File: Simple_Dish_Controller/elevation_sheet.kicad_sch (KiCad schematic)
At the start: 20 parts, among them J2 1-Pin Terminal Block, J7 RJ45 port shielded, RA, TH, J8 RJ45 port shielded, RA, TH, Q1 PZT2222A, Q2 PZT2222A, SW2 SW_SPDT_312, U2 74LS08, U3 74LS32, U4 NE555PS

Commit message: Still creating parts libraries
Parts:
- removed SW2: SW_SPDT_312, SPDT-90-Deg-On-Off-On:B18JH, symbol Switch:SW_SPDT_312
- added J6: Conn_01x03_Pin, DishFootprints:PinHeader_1x03_P2.54mm_Vertical, symbol DishSymbols:Conn_01x03_Pin
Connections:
- net +5V: now also J6.2
- net Dir Sig: now also J6.1
- net at R5.1, U2.5: now also J6.3
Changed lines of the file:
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@@
+	(wire
+		(pts
+			(xy 54.61 58.42) (xy 54.61 67.31)
+		)
+		(stroke
+			(width 0)
+			(type default)
+		)
+	)
 	(wire
 		(pts
@@
 	(wire
 		(pts
+			(xy 52.07 67.31) (xy 54.61 67.31)
+		)
+		(stroke
+			(width 0)
+			(type default)
+		)
+	)
+	(wire
+		(pts
 			(xy 228.6 53.34) (xy 236.22 53.34)
 		)
@@
 	(wire
 		(pts
-			(xy 48.26 67.31) (xy 43.18 67.31)
-		)
-		(stroke
-			(width 0)
-			(type default)
-		)
-	)
-	(wire
-		(pts
 			(xy 96.52 66.04) (xy 104.14 66.04)
 		)
@@
 	(wire
 		(pts
+			(xy 52.07 69.85) (xy 58.42 69.85)
+		)
+		(stroke
+			(width 0)
+			(type default)
+		)
+	)
+	(wire
+		(pts
 			(xy 195.58 50.8) (xy 195.58 52.07)
 		)
@@
 	(wire
 		(pts
+			(xy 52.07 64.77) (xy 58.42 64.77)
+		)
+		(stroke
+			(width 0)
+			(type default)
+		)
+	)
+	(wire
+		(pts
 			(xy 232.41 82.55) (xy 238.76 82.55)
 		)
@@
 		(pts
 			(xy 214.63 137.16) (xy 214.63 139.7)
-		)
-		(stroke
-			(width 0)
-			(type default)
-		)
-	)
-	(wire
-		(pts
-			(xy 43.18 67.31) (xy 43.18 62.23)
 		)
 		(stroke
@@
 	(symbol
 		(lib_id "power:+5V")
-		(at 43.18 62.23 0)
+		(at 54.61 58.42 0)
 		(unit 1)
 		(exclude_from_sim no)
@@
 		(dnp no)
 		(property "Reference" "#PWR09"
-			(at 43.18 66.04 0)
+			(at 54.61 62.23 0)
 			(effects
 				(font
@@
 		)
 		(property "Value" "+5V"
-			(at 43.18 58.42 0)
+			(at 54.61 54.61 0)
 			(effects
 				(font
@@
 		)
 		(property "Footprint" ""
-			(at 43.18 62.23 0)
+			(at 54.61 58.42 0)
 			(effects
 				(font
@@
 		)
 		(property "Datasheet" ""
-			(at 43.18 62.23 0)
+			(at 54.61 58.42 0)
 			(effects
 				(font
@@
 		)
 		(property "Description" "Power symbol creates a global label with name \"+5V\""
-			(at 43.18 62.23 0)
+			(at 54.61 58.42 0)
 			(effects
 				(font
@@
 	)
 	(symbol
+		(lib_id "DishSymbols:Conn_01x03_Pin")
+		(at 46.99 67.31 0)
+		(unit 1)
+		(exclude_from_sim no)
+		(in_bom yes)
+		(on_board yes)
+		(dnp no)
+		(property "Reference" "J6"
+			(at 46.99 62.23 0)
+			(effects
+				(font
+					(size 1.27 1.27)
+				)
+			)
+		)
+		(property "Value" "Conn_01x03_Pin"
+			(at 46.99 72.39 0)
+			(effects
+				(font
+					(size 1.27 1.27)
+				)
+			)
+		)
+		(property "Footprint" "DishFootprints:PinHeader_1x03_P2.54mm_Vertical"
+			(at 46.99 67.31 0)
+			(effects
+				(font
+					(size 1.27 1.27)
+				)
+				(hide yes)
+			)
+		)
+		(property "Datasheet" "~https://app.adam-tech.com/products/download/data_sheet/201605/ph1-xx-ua-data-sheet.pdf"
+			(at 46.99 67.31 0)
+			(effects
+				(font
+					(size 1.27 1.27)
+				)
+				(hide yes)
+			)
+		)
+		(property "Description" "Connector Header Through Hole 3 position 0.100\" (2.54mm)"
+			(at 46.99 67.31 0)
+			(effects
+				(font
+					(size 1.27 1.27)
+				)
+				(hide yes)
+			)
+		)
+		(property "Package" "-"
+			(at 46.99 67.31 0)
+			(effects
+				(font
+					(size 1 1)
+				)
+				(hide yes)
+			)
+		)
+		(property "MF" "Adam Tech"
+			(at 46.99 67.31 0)
+			(effects
+				(font
+					(size 1 1)
+				)
+				(hide yes)
+			)
+		)
+		(property "MPN" "PH1-03-UA"
+			(at 46.99 67.31 0)
+			(effects
+				(font
+					(size 1 1)
+				)
+				(hide yes)
+			)
+		)
+		(property "DIS" "Digikey"
+			(at 46.99 67.31 0)
+			(effects
+				(font
+					(size 1 1)
+				)
+				(hide yes)
+			)
+		)
+		(property "DPN" "2057-PH1-03-UA-ND"
+			(at 46.99 67.31 0)
+			(effects
+				(font
+					(size 1 1)
+				)
+				(hide yes)
+			)
+		)
+		(property "Purchase_URL" "https://www.digikey.com/en/products/detail/adam-tech/PH1-03-UA/9830289"
+			(at 46.99 67.31 0)
+			(effects
+				(font
+					(size 1 1)
+				)
+				(hide yes)
+			)
+		)
+		(property "Price" "0.04"
+			(at 46.99 67.31 0)
+			(effects
+				(font
+					(size 1 1)
+				)
+				(hide yes)
+			)
+		)
+		(property "Note" ""
+			(at 46.99 67.31 0)
+			(effects
+				(font
+					(size 1 1)
+				)
+				(hide yes)
+			)
+		)
+		(pin "3"
+		)
+		(pin "1"
+		)
+		(pin "2"
+		)
+		(instances
+			(project ""
+				(path "/8648ccd3-30ce-4b98-baff-aeab56a7c9f5/a4809f50-064d-4cb7-b1f7-56bf09fb0ea4"
+					(reference "J6")
+					(unit 1)
+				)
+			)
+		)
+	)
+	(symbol
 		(lib_id "power:GND")
 		(at 69.85 172.72 0)
@@
 					(unit 1)
 				)
-			)
-		)
-	)
-	(symbol
-		(lib_id "Switch:SW_SPDT_312")
-		(at 53.34 67.31 0)
-		(unit 1)
-		(exclude_from_sim no)
-		(in_bom yes)
-		(on_board yes)
-		(dnp no)
-		(property "Reference" "SW2"
-			(at 53.34 62.23 0)
-			(effects
-				(font
-					(size 1.27 1.27)
-				)
-			)
-		)
-		(property "Value" "SW_SPDT_312"
-			(at 53.34 60.96 0)
-			(effects
-				(font
-					(size 1.27 1.27)
-				)
-				(hide yes)
-			)
-		)
-		(property "Footprint" "SPDT-90-Deg-On-Off-On:B18JH"
-			(at 53.34 77.47 0)
-			(effects
-				(font
-					(size 1.27 1.27)
-				)
-				(hide yes)
-			)
-		)
-		(property "Datasheet" "~"
-			(at 53.34 74.93 0)
-			(effects
-				(font
-					(size 1.27 1.27)
-				)
-				(hide yes)
-			)
-		)
-		(property "Description" "Switch, single pole double throw"
-			(at 53.34 67.31 0)
-			(effects
-				(font
-					(size 1.27 1.27)
-				)
-				(hide yes)
-			)
-		)
-		(property "LCSC Part" ""
-			(at 53.34 67.31 0)
-			(effects
-				(font
-					(size 1.27 1.27)
-				)
-			)
-		)
-		(pin "2"
-		)
-		(pin "1"
-		)
-		(pin "3"
-		)
-		(instances
-			(project "simple_dish_manual_controller"
-				(path "/8648ccd3-30ce-4b98-baff-aeab56a7c9f5/a4809f50-064d-4cb7-b1f7-56bf09fb0ea4"
-					(reference "SW2")
-					(unit 1)
-				)

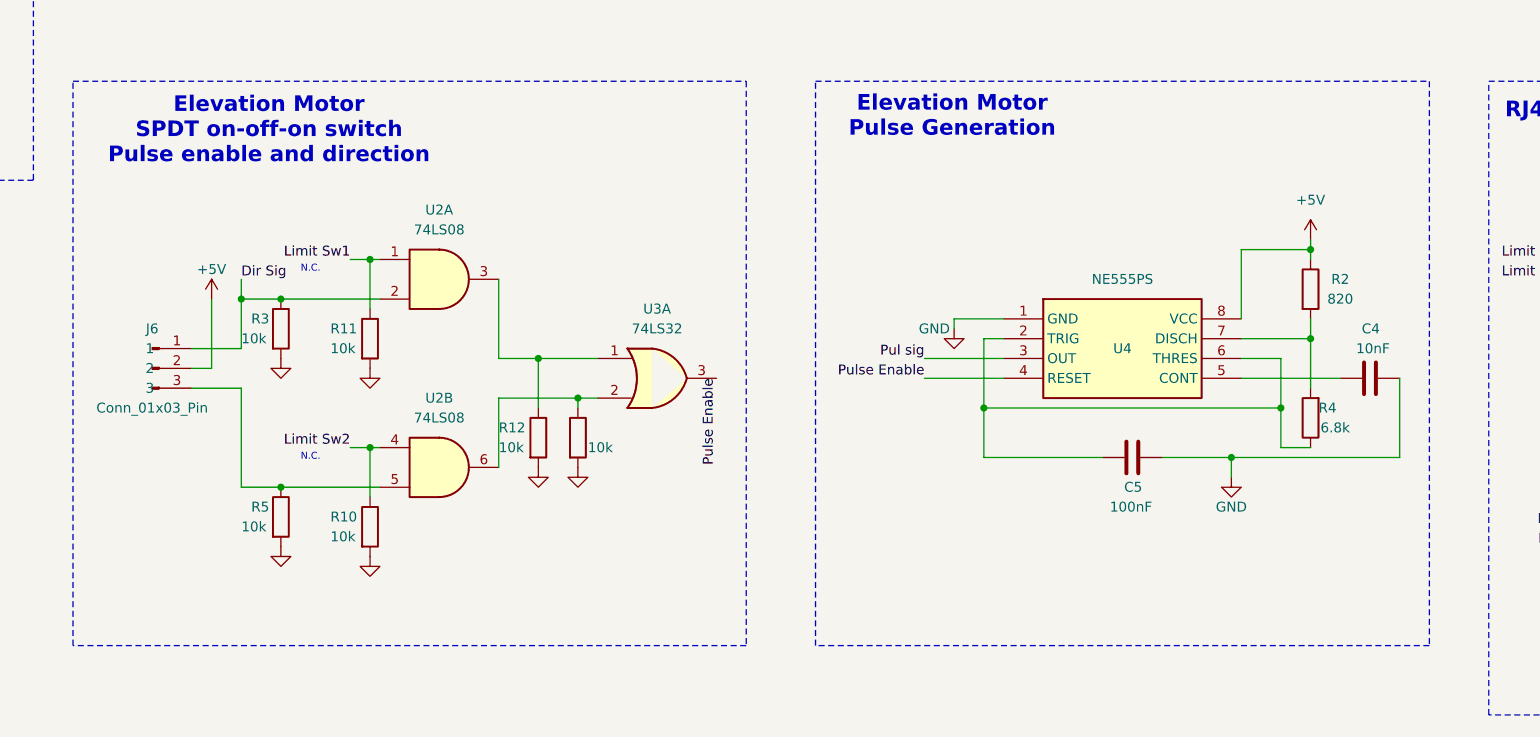
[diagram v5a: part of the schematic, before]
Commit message: More parts defined
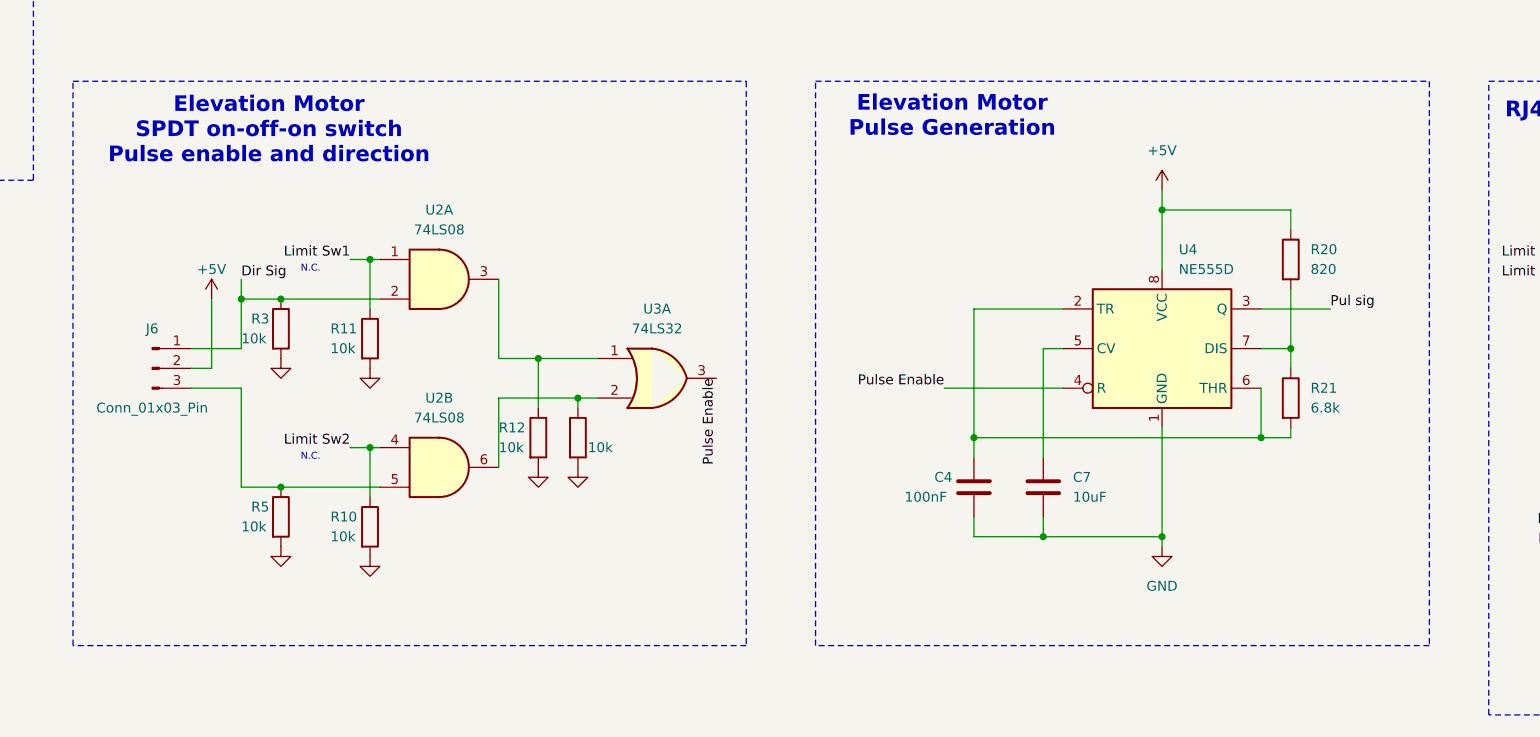
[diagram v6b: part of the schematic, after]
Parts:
- removed C4: 10nF, Capacitor_SMD:C_0805_2012Metric, symbol Device:C
- removed C5: 100nF, Capacitor_SMD:C_0805_2012Metric, symbol Device:C
- removed R2: 820, Resistor_SMD:R_0805_2012Metric, symbol Device:R
- removed R4: 6.8k, Resistor_SMD:R_0805_2012Metric, symbol Device:R
- removed U4: NE555PS, NE555P Osc Chip SMD:SOIC127P780X200-8N, symbol NE555P Osc Chip SMD:NE555PS
- added C4: 100nF, DishFootprints:C_0805, symbol DishSymbols:CAP 100nF 0805
- added C7: 10uF, DishFootprints:C_0805, symbol DishSymbols:CAP 10nF 0805
- added R20: 820, DishFootprints:R_0805, symbol DishSymbols:RES 820 0805
- added R21: 6.8k, DishFootprints:R_0805, symbol DishSymbols:RES 6.8k 0805
- added U4: NE555D, DishFootprints:SOIC-8_3.9x4.9mm_P1.27mm, symbol DishSymbols:NE555D
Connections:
- net +5V: now also R20.1, U4.8 (VCC)
- net GND: now also C4.2, C7.2, U4.1 (GND)
- net Pul sig: now also U4.3 (Q)
- net Pulse Enable: now also U4.4 (R)
- new net: R20.2, R21.1, U4.7 (DIS)
- new net: C4.1, R21.2, U4.2 (TR), U4.6 (THR)
- new net: C7.1, U4.5 (CV)

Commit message: Latest update
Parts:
- removed J2: 1-Pin Terminal Block, 1-Pin Barrier Terminal Block:RHDR1W160P0X826_1X1_1020X1270X1270P, symbol 1-Pin Barrier Terminal Block:38700-6301
- removed J7, J8: RJ45 port shielded, RA, TH, DishController_footprints:RJ45 Port Shielded, Right Angle TH, symbol DishController_symbols:RJ45 port shielded, Right Angle TH
- removed Q1, Q2: PZT2222A, Package_TO_SOT_SMD:SOT-223-3_TabPin2, symbol Transistor_BJT:PZT2222A
- removed U2: 74LS08, 74LS08_SOIC:SOIC127P600X175-14N, symbol 74xx:74LS08
- removed U3: 74LS32, 74LS32_SOIC:SOIC127P600X175-14N, symbol 74xx:74LS32
- added J5: DE-15_VGA_FEMALE_CONN, DishFootprintsSupplier:DB15_VGA_FEMALE_CONN, symbol DishSymbolsSupplier:DE-15_VGA_FEMALE_CONN
- added Q1, Q5: PZT2222A, DishFootprints:SOT-223, symbol DishSymbols:PZT2222A
- added U2: 74LS08, DishFootprints:SOIC-14_3.9x8.7mm_P1.27mm, symbol DishSymbols:74LS08
- added U3: 74LS32, DishFootprints:SOIC-14_3.9x8.7mm_P1.27mm, symbol DishSymbols:74LS32
- R13: footprint Resistor_SMD:R_0805_2012Metric -> DishFootprints:R_0805
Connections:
- net +5V: now also J5.1
- net Dir: now also J5.12, Q5.2 (C)
- net Dir Sig: now also U2.2
- net GND: now also J5.2, Q1.3 (E), Q5.3 (E)
- net Limit Sw1: now also J5.3, U2.1
- net Limit Sw2: now also J5.4, U2.4
- net Pul: now also J5.11, Q1.2 (C)
- net Pul sig: now also Q1.1 (B)
- net Pulse Enable: now also U3.3
- net Shield: now also J5.SH1 (SHIELD), J5.SH2 (SHIELD)
- net at R13.1: now also U2.6, U3.2
- net at J6.3, R5.1: now also U2.5
- net at R6.2: now also Q5.1 (B)
- net at R12.1: now also U2.3, U3.1
- no-connect marks 22 -> 9
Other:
- note removed: "Connect to Chassis"
- note removed: "Logic Chips Power and Gnd"
- note removed: "Shield to Chassis"
- note removed: "Unused from Quad chip"
- moved on the sheet: R6

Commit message: Updates
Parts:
- removed C4: 100nF, DishFootprints:C_0805, symbol DishSymbols:CAP 100nF 0805
- removed C7: 10uF, DishFootprints:C_0805, symbol DishSymbols:CAP 10nF 0805
- removed J5: DE-15_VGA_FEMALE_CONN, DishFootprintsSupplier:DB15_VGA_FEMALE_CONN, symbol DishSymbolsSupplier:DE-15_VGA_FEMALE_CONN
- removed J6: Conn_01x03_Pin, DishFootprints:PinHeader_1x03_P2.54mm_Vertical, symbol DishSymbols:Conn_01x03_Pin
- removed Q1, Q5: PZT2222A, DishFootprints:SOT-223, symbol DishSymbols:PZT2222A
- removed R11, R12: 10k, Resistor_SMD:R_0805_2012Metric, symbol Device:R
- removed R13: 10k, DishFootprints:R_0805, symbol Device:R
- removed R20: 820, DishFootprints:R_0805, symbol DishSymbols:RES 820 0805
- removed R21: 6.8k, DishFootprints:R_0805, symbol DishSymbols:RES 6.8k 0805
- removed U2: 74LS08, DishFootprints:SOIC-14_3.9x8.7mm_P1.27mm, symbol DishSymbols:74LS08
- removed U3: 74LS32, DishFootprints:SOIC-14_3.9x8.7mm_P1.27mm, symbol DishSymbols:74LS32
- removed U4: NE555D, DishFootprints:SOIC-8_3.9x4.9mm_P1.27mm, symbol DishSymbols:NE555D
- added C5: 0.1uF, Capacitor_SMD:C_1206_3216Metric, symbol Device:C
- added C6: 100nF, Capacitor_SMD:C_1206_3216Metric, symbol Device:C
- added C7: 10uF, Capacitor_SMD:C_1206_3216Metric, symbol Device:C
- added J4: Conn_01x03_Pin, Connector_PinHeader_2.54mm:PinHeader_1x03_P2.54mm_Vertical, symbol Connector:Conn_01x03_Pin
- added J5: Elevation DE-15, DishFootprints:DE15_VGA_FEMALE_CONN, symbol DishSymbols:DE-15_VGA_FEMALE_CONN
- added Q1, Q2: MMBT2222A, Package_TO_SOT_SMD:SOT-23, symbol Transistor_BJT:MMBT2222A
- added R2: 820, Resistor_SMD:R_1206_3216Metric, symbol Device:R
- added R4, R7, R8, R9: 10k, Resistor_SMD:R_1206_3216Metric, symbol Device:R
- added U2: 74LS32, Package_SO:SOIC-14_3.9x8.7mm_P1.27mm, symbol 74xx:74LS32
- added U3: 74LS08, Package_SO:SOIC-14_3.9x8.7mm_P1.27mm, symbol 74xx:74LS08
- added U4: NE555D, Package_SO:SOIC-8_3.9x4.9mm_P1.27mm, symbol Timer:NE555D
- R10: value 10k -> 1k; footprint Resistor_SMD:R_0805_2012Metric -> Resistor_SMD:R_1206_3216Metric
- R3: footprint Resistor_SMD:R_0805_2012Metric -> Resistor_SMD:R_1206_3216Metric
- R5: value 10k -> 6.8k; footprint Resistor_SMD:R_0805_2012Metric -> Resistor_SMD:R_1206_3216Metric
- R6: value 1k -> 10k; footprint Resistor_SMD:R_0805_2012Metric -> Resistor_SMD:R_1206_3216Metric
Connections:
- net +5V: now also C5.1, J4.2 (Pin_2), J5.1, R2.2, U4.8 (VCC)
- net Dir: now also J5.12, Q1.3 (C)
- net Dir Sig: now also R10.1, J4.1 (Pin_1), U3.2; no longer R6.1
- net GND: now also R6.2, C5.2, C6.2, C7.2, J5.2, Q1.2 (E), Q2.2 (E), R4.2, R7.2, R8.2, R9.2, U4.1 (GND); no longer R10.2, R5.2
- net Limit Sw1: now also J5.3, R4.1, U3.1
- net Limit Sw2: now also J5.4, R9.1, U3.4; no longer R10.1
- net Pul: now also J5.11, Q2.3 (C)
- net Pul sig: now also Q2.1 (B), U4.3 (Q)
- net Pulse Enable: now also U2.3, U4.4 (R)
- net Shield: now also J5.SH1 (SHIELD), J5.SH2 (SHIELD)
- net at R5.1: now also C6.1, U4.2 (TR), U4.6 (THR)
- new net: J4.3 (Pin_3), R8.1, U3.5
- new net: R6.1, U2.1, U3.3
- new net: R7.1, U2.2, U3.6
- new net: R2.1, R5.2, U4.7 (DIS)
- new net: Q1.1 (B), R10.2
- new net: C7.1, U4.5 (CV)
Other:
- note added: "DE-15 Connector"
- note removed: "RJ45 Ports"
